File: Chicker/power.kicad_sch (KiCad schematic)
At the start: 43 parts, among them U11 MCP6231UT-E/OT, U3 AMS1117-3.3

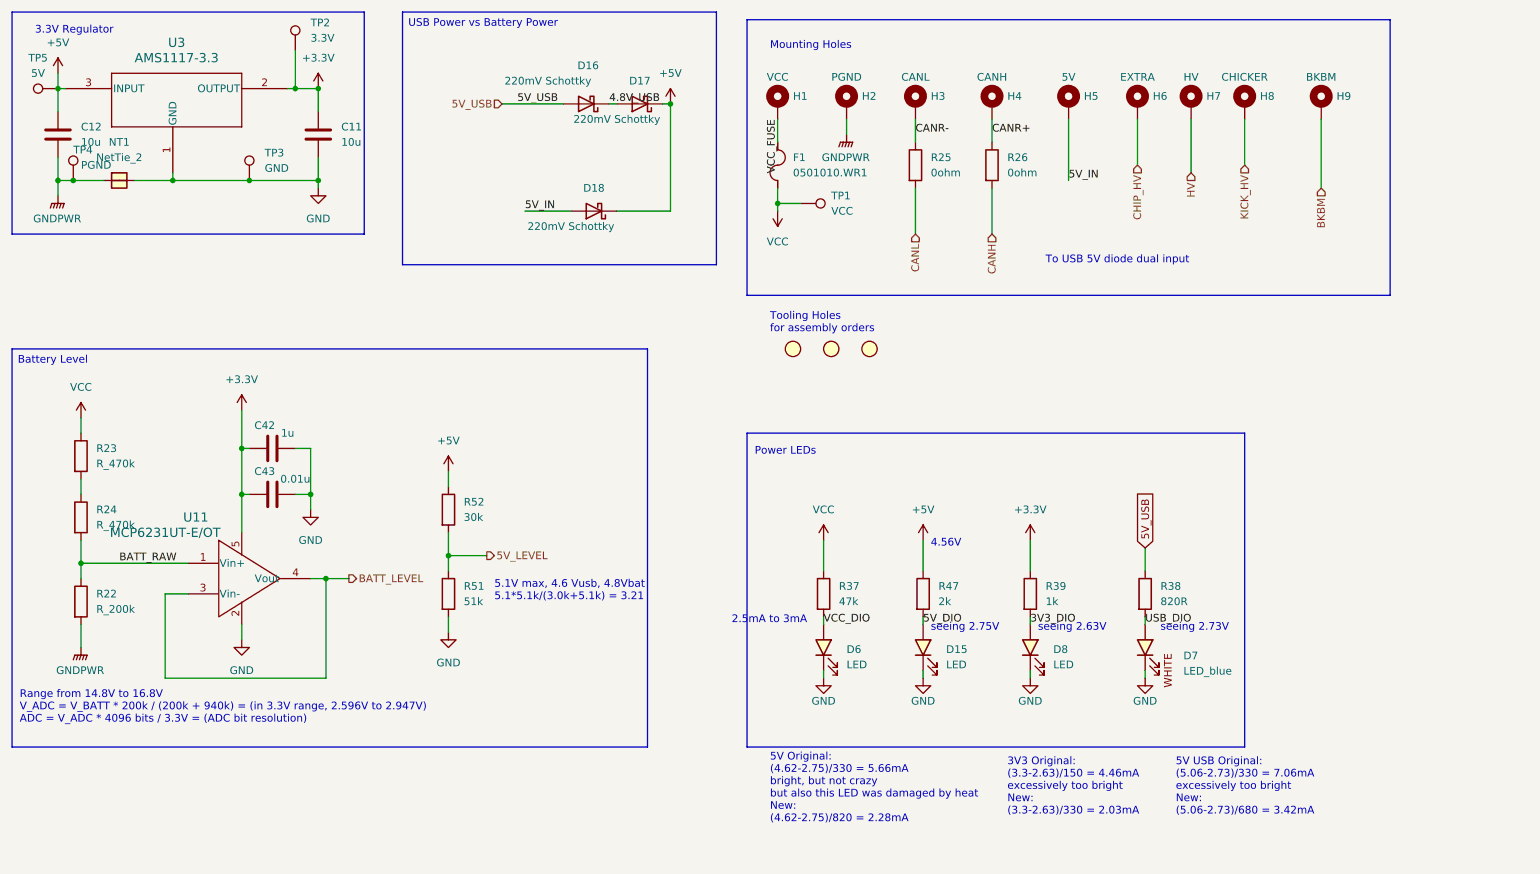
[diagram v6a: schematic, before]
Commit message: changed more to basic
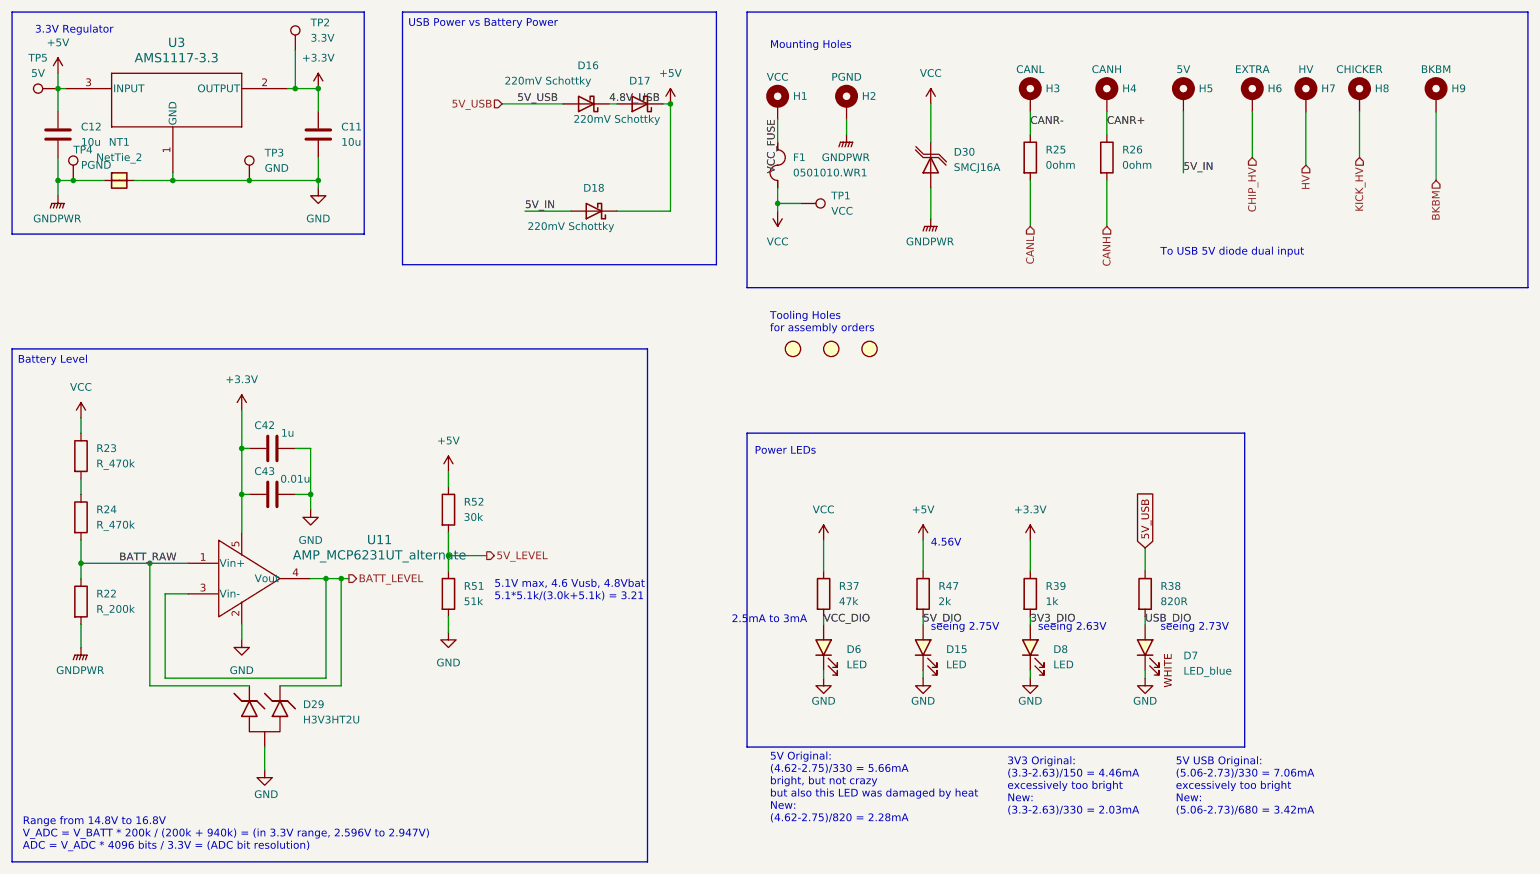
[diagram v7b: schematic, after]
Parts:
- removed U11: MCP6231UT-E/OT, bots:SOT-23-5, symbol thebots_symlib:MCP6231UT-E/OT
- added D29: H3V3HT2U, bots:SOT-723, symbol bots:D_TVS_ESD
- added D30: SMCJ16A, bots:D_SMC, symbol bots:D_SMCJ16A
- added U11: AMP_MCP6231UT_alternate, bots:SOT-23-5, symbol bots:AMP_MCP6231UT_alternate
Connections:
- net +3.3V: now also U11.5
- net BATT_LEVEL: now also D29.1, U11.3 (Vin-), U11.4 (Vout)
- net BATT_RAW: now also D29.2, U11.1 (Vin+)
- net GND: now also D29.3, U11.2
- net GNDPWR: now also D30.2 (A)
- net VCC: now also D30.1 (K)
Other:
- moved on the sheet: H3, H4, H5, H6, H7, H8, H9, R25, R26

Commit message: chicker v1.1 ordered!
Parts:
- D29: footprint bots:SOT-723 -> bots:SOT-23
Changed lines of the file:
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@@
 			)
 		)
-		(property "Description" ""
+		(property "Description" "Resistor"
 			(at 193.04 49.53 0)
 			(effects
@@
 			)
 		)
-		(property "Description" ""
+		(property "Description" "Resistor"
 			(at 205.74 49.53 0)
 			(effects
@@
 			)
 		)
-		(property "Footprint" "bots:SOT-723"
+		(property "Footprint" "bots:SOT-23"
 			(at 59.69 144.78 0)
 			(effects
